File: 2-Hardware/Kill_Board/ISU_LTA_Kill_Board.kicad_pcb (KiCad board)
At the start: 2 copper layers, 157.5 x 36.2 mm, 38 parts, among them P1 CONN_01X02, P10 CONN_2, P11 CONN_2, P12 CONN_2, P13 CONN_2, P2 CONN_01X02, P3 CONN_01X02, P4 CONN_01X03, P5 CONN_01X03, P6 CONN_01X03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

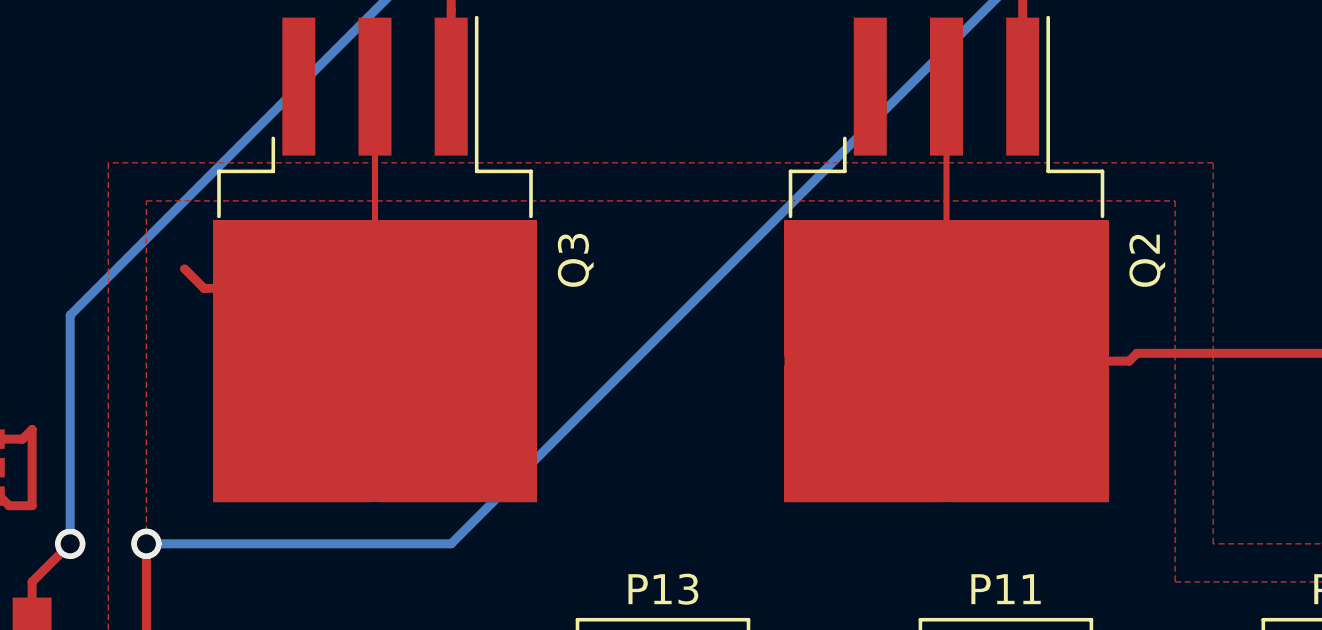
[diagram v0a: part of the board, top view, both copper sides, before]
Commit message: Fixed some of the power plane issues. forgot to update them to solid for the power planes. gnd was already fixed.
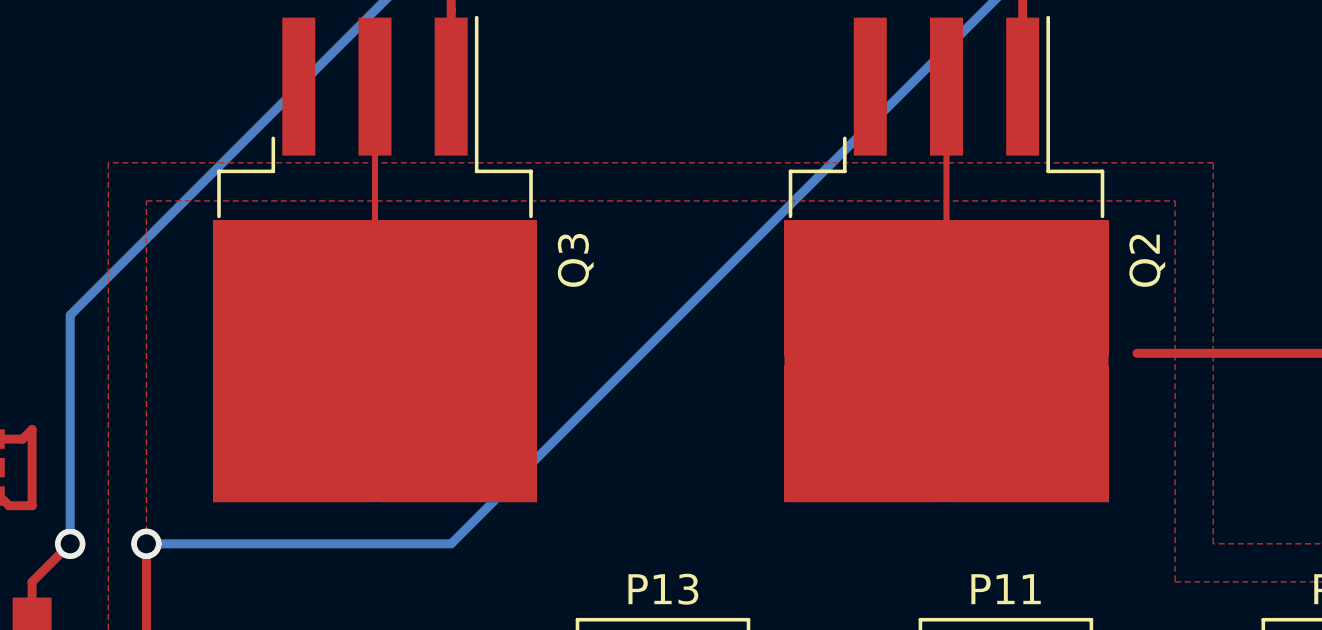
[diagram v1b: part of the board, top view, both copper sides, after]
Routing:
- net /High_Side: track 36.1 -> 25.8 mm
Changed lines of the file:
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@@
     (thickness 1.6002)
     (drawings 5)
-    (tracks 222)
+    (tracks 218)
     (zones 0)
     (modules 38)
@@
   (segment (start 140.97 73.66) (end 140.97 82.81) (width 0.2032) (layer Front) (net 4) (status 30))
   (segment (start 154.78 82.55) (end 147.32 82.55) (width 0.3) (layer Front) (net 4))
-  (segment (start 147.06 82.81) (end 140.97 82.81) (width 0.3) (layer Front) (net 4))
-  (segment (start 147.32 82.55) (end 147.06 82.81) (width 0.3) (layer Front) (net 4))
-  (segment (start 116.22 80.385) (end 115.57 79.735) (width 0.3) (layer Front) (net 4))
-  (segment (start 119.145 80.385) (end 116.22 80.385) (width 0.3) (layer Front) (net 4))
   (segment (start 68.420392 78.74) (end 69.77 78.74) (width 0.3) (layer Front) (net 5))
   (segment (start 59.638099 69.957707) (end 68.420392 78.74) (width 0.3) (layer Front) (net 5))
@@
   )
   (zone (net 1) (net_name +3.3V) (layer Back) (hatch edge 0.508)
-    (connect_pads (clearance 0.2032))
+    (connect_pads yes (clearance 0.2032))
     (min_thickness 0.254)
     (fill yes (arc_segments 16) (thermal_gap 0.508) (thermal_bridge_width 0.508))
@@
   )
   (zone (net 6) (net_name GND) (layer Front) (hatch edge 0.508)
-    (connect_pads (clearance 0.2032))
+    (connect_pads yes (clearance 0.2032))
     (min_thickness 0.254)
     (fill yes (arc_segments 16) (thermal_gap 0.508) (thermal_bridge_width 0.508))
@@
   )
   (zone (net 24) (net_name +5V) (layer Back) (hatch edge 0.508)
-    (connect_pads (clearance 0.2032))
+    (connect_pads yes (clearance 0.2032))
     (min_thickness 0.254)
     (fill yes (arc_segments 16) (thermal_gap 0.508) (thermal_bridge_width 0.508))

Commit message: New Revision
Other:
- net class Default removed
